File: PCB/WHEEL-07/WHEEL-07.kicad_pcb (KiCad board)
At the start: 2 copper layers, 11 parts, among them U1 STM32F405RGTx, Y1 16Mhz, Y2 32KHz

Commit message: Finished schematics
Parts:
- added C12: 0,1mF, Capacitor_SMD:C_0805_2012Metric, F.Cu at (103.8, 115.5)
- added C13: 1uF, Capacitor_SMD:C_0805_2012Metric, F.Cu at (127.5, 92.5)
- added C14: 4.7uF, Capacitor_SMD:C_0805_2012Metric, F.Cu at (127.5, 95.5)
- added IC1: TS5A21366DCUR, PDM_Additional:SOP50P310X90-8N, F.Cu at (104.4, 112.2)
- added R2: 2k2, Resistor_SMD:R_0402_1005Metric_Pad0.72x0.64mm_HandSolder, F.Cu at (109.2, 100.2)
- added R3: 2k2, Resistor_SMD:R_0402_1005Metric_Pad0.72x0.64mm_HandSolder, F.Cu at (116.5, 92.0)
- added R4: 120, Resistor_SMD:R_0402_1005Metric, F.Cu at (107.5, 115.0)
- added R5: 1k5, Resistor_SMD:R_0402_1005Metric_Pad0.72x0.64mm_HandSolder, F.Cu at (114.3, 96.8)
- added R6: 120, Resistor_SMD:R_0402_1005Metric, F.Cu at (103.1, 118.0)
- added U2: MCP2561-E-SN, Package_SO:SOIC-8_3.9x4.9mm_P1.27mm, F.Cu at (97.4, 113.6)
- added U3: MCP2561-E-SN, Package_SO:SOIC-8_3.9x4.9mm_P1.27mm, F.Cu at (97.4, 120.0)
- moved C8 54.5 mm to (119.7, 92.0)
- moved C4 51.2 mm to (119.7, 94.0)
- moved C3 44.7 mm to (109.2, 104.1)
- moved R1 44.7 mm to (116.5, 94.0)
- moved Y2 44.4 mm to (110.1, 97.5)
- moved U1 44.4 mm to (100.4, 98.2)
- moved Y1 44.4 mm to (111.2, 93.4)
- moved C9 43.0 mm to (117.5, 96.0)
- moved C7 41.8 mm to (112.5, 100.2)
- moved C5 40.8 mm to (112.5, 102.2)
- moved C6 40.6 mm to (109.2, 102.2)
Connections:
- U1 pad 10: unconnected-(U1-Pad10) -> ADC_A3
- U1 pad 11: unconnected-(U1-Pad11) -> ADC_A4
- U1 pad 14: unconnected-(U1-Pad14) -> ADC_B1
- U1 pad 15: unconnected-(U1-Pad15) -> ADC_B2
- U1 pad 16: unconnected-(U1-Pad16) -> ADC_B3
- U1 pad 17: unconnected-(U1-Pad17) -> ADC_B4
- U1 pad 2: unconnected-(U1-Pad2) -> LED_STATUS
- U1 pad 20: unconnected-(U1-Pad20) -> GPIO_1
- U1 pad 21: unconnected-(U1-Pad21) -> GPIO_2
- U1 pad 22: unconnected-(U1-Pad22) -> GPIO_3
- U1 pad 23: unconnected-(U1-Pad23) -> GPIO_4
- U1 pad 24: unconnected-(U1-Pad24) -> GPIO_5
- U1 pad 25: unconnected-(U1-Pad25) -> GPIO_6
- U1 pad 26: unconnected-(U1-Pad26) -> GPIO_7
- U1 pad 27: unconnected-(U1-Pad27) -> GPIO_8
- U1 pad 29: unconnected-(U1-Pad29) -> I2C2_SCL
- U1 pad 3: unconnected-(U1-Pad3) -> OSC32_IN
- U1 pad 30: unconnected-(U1-Pad30) -> I2C2_SDA
- U1 pad 34: unconnected-(U1-Pad34) -> SPI2_SCK
- U1 pad 35: unconnected-(U1-Pad35) -> SPI2_MISO
- U1 pad 36: unconnected-(U1-Pad36) -> SPI2_MOSI
- U1 pad 4: unconnected-(U1-Pad4) -> OSC32_OUT
- U1 pad 41: unconnected-(U1-Pad41) -> TIM1_CH1
- U1 pad 42: unconnected-(U1-Pad42) -> TIM1_CH2
- U1 pad 43: unconnected-(U1-Pad43) -> TIM1_CH3
- U1 pad 51: unconnected-(U1-Pad51) -> USART_TX
- U1 pad 52: unconnected-(U1-Pad52) -> USART_RX
- U1 pad 53: unconnected-(U1-Pad53) -> USART_CK
- U1 pad 57: unconnected-(U1-Pad57) -> CAN2_RX
- U1 pad 58: unconnected-(U1-Pad58) -> CAN2_TX
- U1 pad 61: unconnected-(U1-Pad61) -> CAN1_RX
- U1 pad 62: unconnected-(U1-Pad62) -> CAN1_TX
- U1 pad 8: unconnected-(U1-Pad8) -> ADC_A1
- U1 pad 9: unconnected-(U1-Pad9) -> ADC_A2

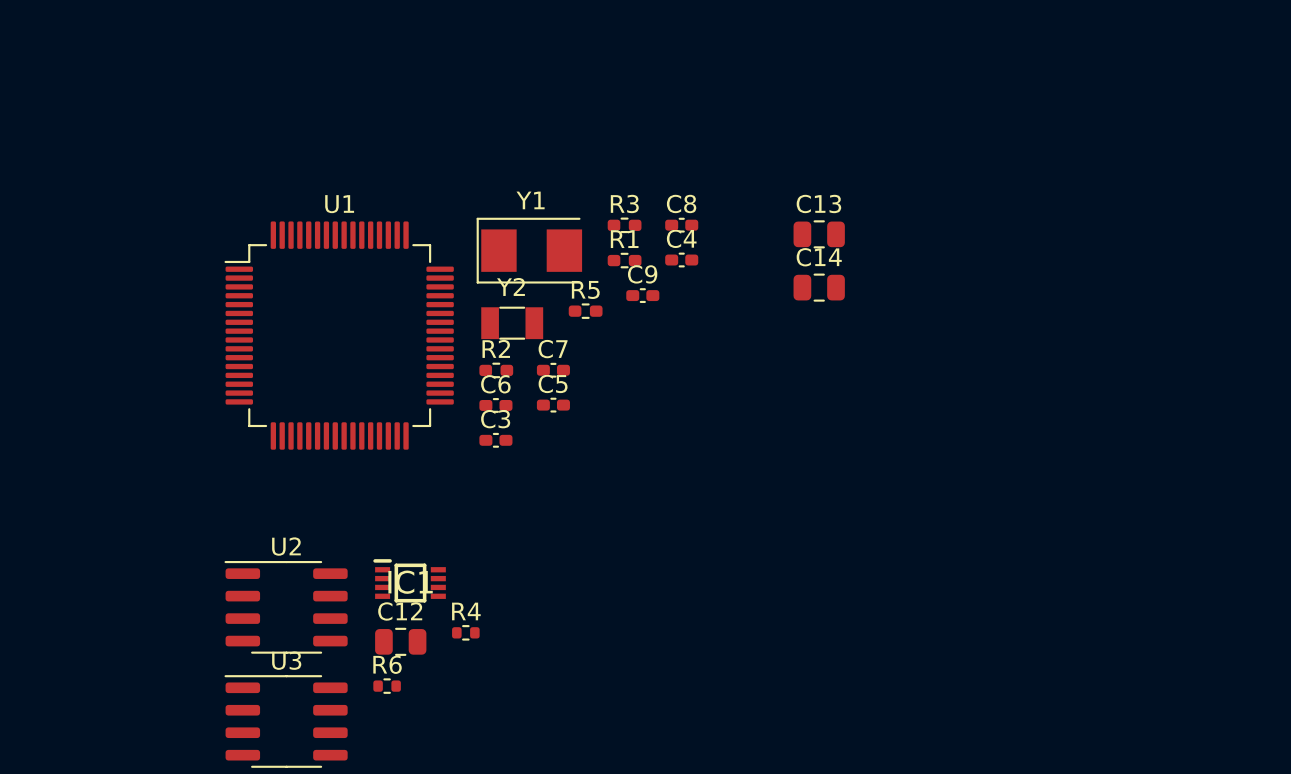
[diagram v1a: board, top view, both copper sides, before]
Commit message: Modified layout
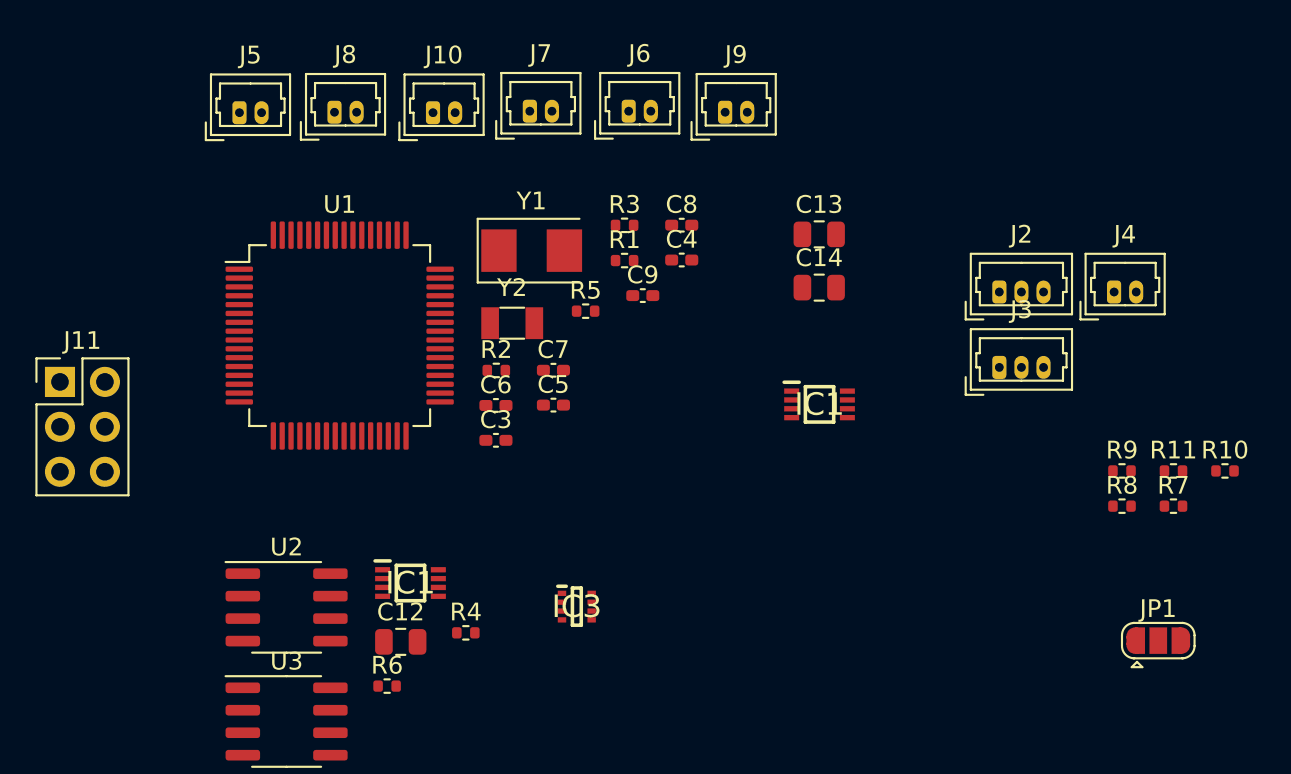
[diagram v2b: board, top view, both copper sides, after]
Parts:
- added IC1: TS5A21366DCUR, PDM_Additional:SOP50P310X90-8N, F.Cu at (127.5, 102.1)
- added IC3: MP2332HGTL-P, WHEEL_07_LIBRARY_LOADER:SOTFL50P160X60-8N, F.Cu at (113.8, 113.5)
- added J10: BUTTON, Connector_Molex:Molex_PicoBlade_53047-0210_1x02_P1.25mm_Vertical, F.Cu at (105.7, 85.6)
- added J11: Conn_02x03_Counter_Clockwise, Connector_PinHeader_2.54mm:PinHeader_2x03_P2.54mm_Vertical, F.Cu at (84.6, 100.8)
- added J2: SPI, Connector_Molex:Molex_PicoBlade_53047-0310_1x03_P1.25mm_Vertical, F.Cu at (137.7, 95.8)
- added J3: USART, Connector_Molex:Molex_PicoBlade_53047-0310_1x03_P1.25mm_Vertical, F.Cu at (137.7, 100.0)
- added J4: I2C, Connector_Molex:Molex_PicoBlade_53047-0210_1x02_P1.25mm_Vertical, F.Cu at (144.2, 95.8)
- added J5: BUTTON, Connector_Molex:Molex_PicoBlade_53047-0210_1x02_P1.25mm_Vertical, F.Cu at (94.7, 85.6)
- added J6: BUTTON, Connector_Molex:Molex_PicoBlade_53047-0210_1x02_P1.25mm_Vertical, F.Cu at (116.7, 85.5)
- added J7: BUTTON, Connector_Molex:Molex_PicoBlade_53047-0210_1x02_P1.25mm_Vertical, F.Cu at (111.1, 85.5)
- added J8: BUTTON, Connector_Molex:Molex_PicoBlade_53047-0210_1x02_P1.25mm_Vertical, F.Cu at (100.1, 85.6)
- added J9: BUTTON, Connector_Molex:Molex_PicoBlade_53047-0210_1x02_P1.25mm_Vertical, F.Cu at (122.2, 85.6)
- added JP1: SolderJumper_3_Open, Jumper:SolderJumper-3_P1.3mm_Open_RoundedPad1.0x1.5mm, F.Cu at (146.7, 115.5)
- added R10: 13k, Resistor_SMD:R_0402_1005Metric, F.Cu at (150.4, 105.9)
- added R11: 40.2k, Resistor_SMD:R_0402_1005Metric, F.Cu at (147.5, 105.9)
- added R7: 200k, Resistor_SMD:R_0402_1005Metric, F.Cu at (147.5, 107.9)
- added R8: 20, Resistor_SMD:R_0402_1005Metric, F.Cu at (144.6, 107.9)
- added R9: 20k, Resistor_SMD:R_0402_1005Metric, F.Cu at (144.6, 105.9)
- R1, R2, R3, R5: footprint Resistor_SMD:R_0402_1005Metric_Pad0.72x0.64mm_HandSolder -> Resistor_SMD:R_0402_1005Metric
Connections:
- C8 pad 1: VDDA -> +3.3VA
- C9 pad 1: VDDA -> +3.3VA
- IC1 pad 3: /CAN_BUS/CAN_TERMINATOR_2 -> CAN2_TERMINATOR_SW
- IC1 pad 7: /CAN_BUS/CAN_TERMINATOR_1 -> CAN1_TERMINATOR_SW
- R4 pad 2: Net-(IC1-Pad1) -> Net-(R4-Pad2)
- R6 pad 2: Net-(IC1-Pad5) -> Net-(R6-Pad2)
- U1 pad 33: unconnected-(U1-Pad33) -> SPI_CS
- U1 pad 37: unconnected-(U1-Pad37) -> TIM1_CH1
- U1 pad 38: unconnected-(U1-Pad38) -> TIM1_CH2
- U1 pad 39: unconnected-(U1-Pad39) -> TIM1_CH3
- U1 pad 56: unconnected-(U1-Pad56) -> CAN2_TERMINATOR_SW
- U1 pad 59: unconnected-(U1-Pad59) -> CAN1_TERMINATOR_SW
- U1 pad 63: unconnected-(U1-Pad63) -> GND

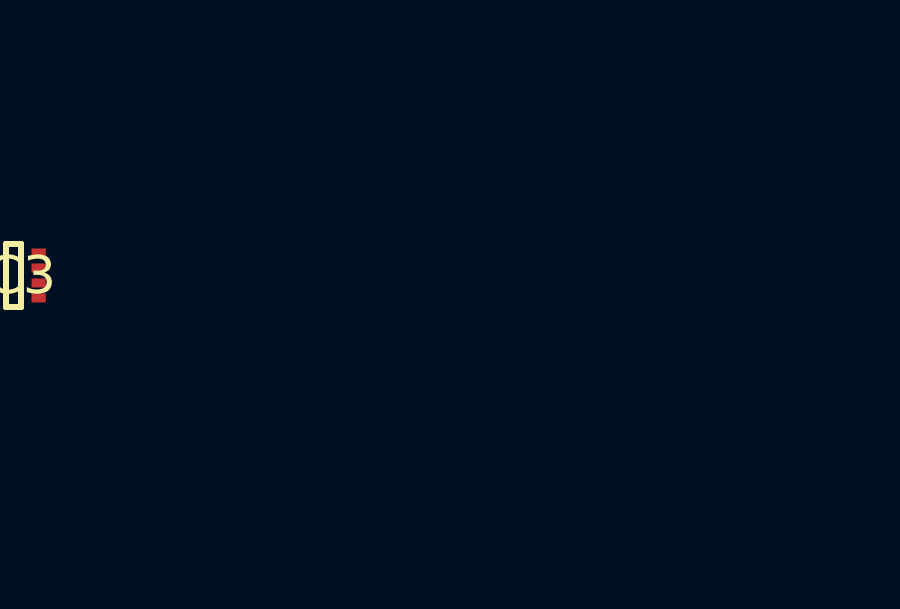
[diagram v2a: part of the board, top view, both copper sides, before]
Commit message: Added paddles hardware debouncing to PCB
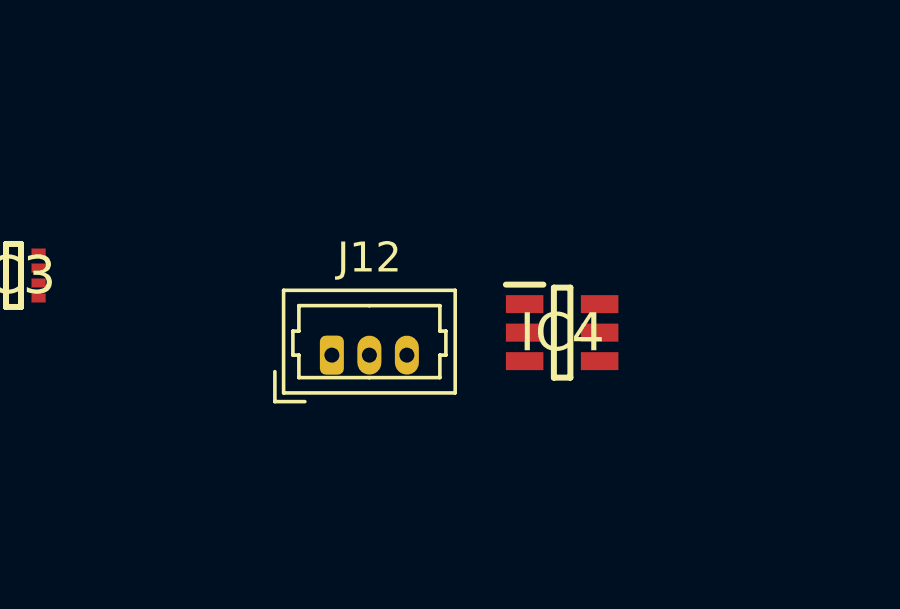
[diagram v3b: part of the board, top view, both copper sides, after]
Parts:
- added IC4: NL27WZ14DTT1G, WHEEL_07_LIBRARY_LOADER:SOT95P275X110-6N, F.Cu at (132.1, 115.4)
- added J12: USART, Connector_Molex:Molex_PicoBlade_53047-0310_1x03_P1.25mm_Vertical, F.Cu at (124.4, 116.2)
- J5: value BUTTON -> PADDLE1
- J6: value BUTTON -> PADDLE2
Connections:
- IC1 pad 1: Net-(R4-Pad2) -> Net-(IC1-Pad1)
- IC1 pad 5: Net-(R6-Pad2) -> Net-(IC1-Pad5)
- J5 pad 2: GPIO_1 -> PADDLE1_IN
- J6 pad 2: GPIO_2 -> PADDLE2_IN
- R4 pad 2: Net-(R4-Pad2) -> Net-(IC1-Pad1)
- R6 pad 2: Net-(R6-Pad2) -> Net-(IC1-Pad5)

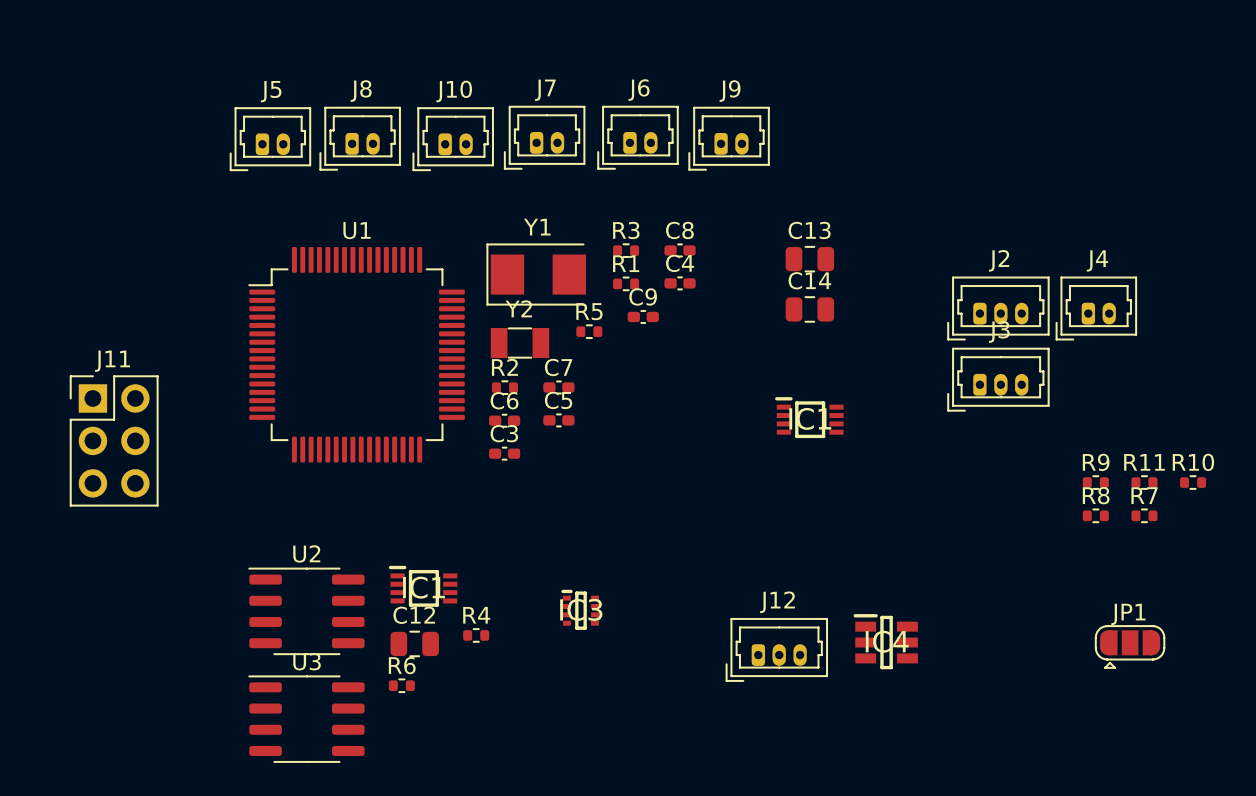
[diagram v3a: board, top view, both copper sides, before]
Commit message: Added rotaries
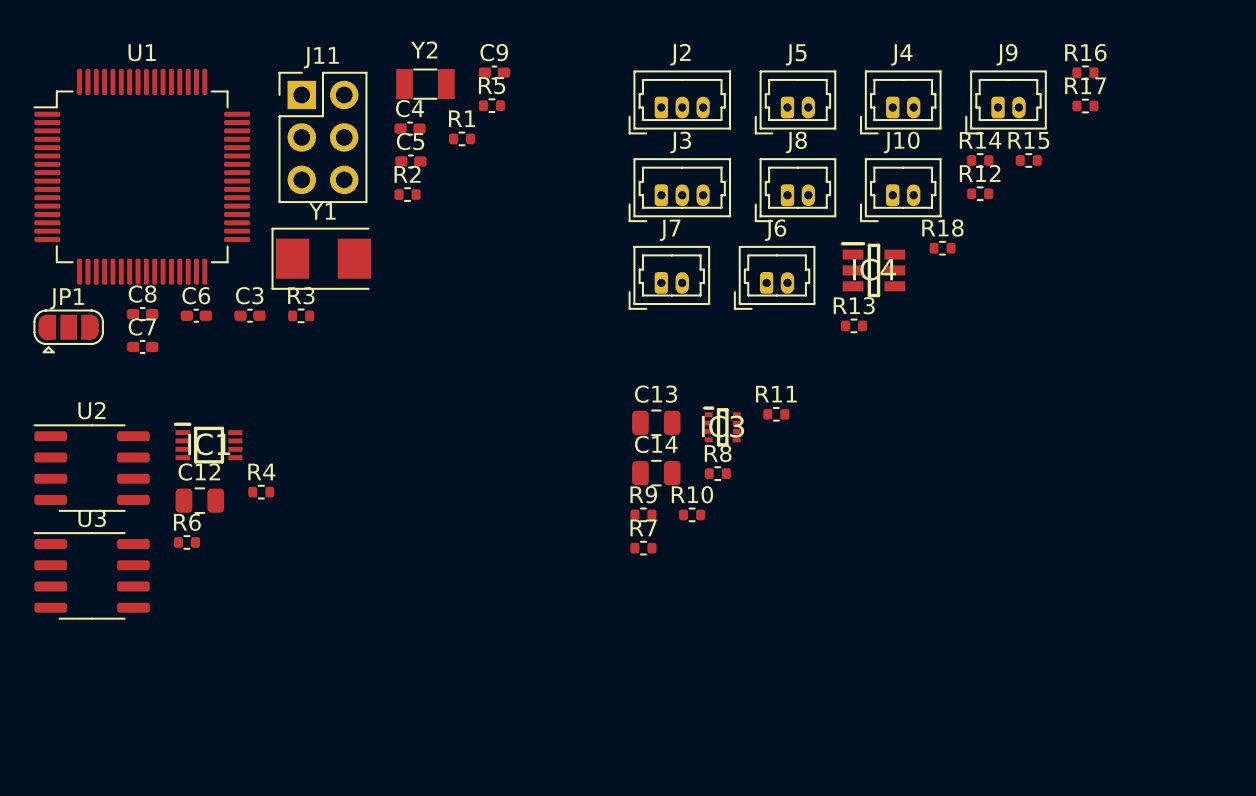
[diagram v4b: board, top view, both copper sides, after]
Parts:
- removed the IC1 at (104.4, 112.2)
- removed the IC1 at (127.5, 102.1)
- removed J12: USART, Connector_Molex:Molex_PicoBlade_53047-0310_1x03_P1.25mm_Vertical
- added IC1: TS5A21366DCUR, PDM_Additional:SOP50P310X90-8N, F.Cu at (91.5, 103.6)
- added R12: 1k, Resistor_SMD:R_0402_1005Metric, F.Cu at (137.7, 88.6)
- added R13: 1k, Resistor_SMD:R_0402_1005Metric, F.Cu at (130.1, 96.5)
- added R14: 10k, Resistor_SMD:R_0402_1005Metric, F.Cu at (137.7, 86.6)
- added R15: 10k, Resistor_SMD:R_0402_1005Metric, F.Cu at (140.6, 86.6)
- added R16: 1k, Resistor_SMD:R_0402_1005Metric, F.Cu at (144.0, 81.3)
- added R17: 1k, Resistor_SMD:R_0402_1005Metric, F.Cu at (144.0, 83.3)
- added R18: 1k, Resistor_SMD:R_0402_1005Metric, F.Cu at (135.4, 91.8)
- moved JP1 66.3 mm to (83.1, 96.6)
- moved C8 32.4 mm to (87.6, 95.8)
- moved J5 31.5 mm to (126.2, 83.4)
- moved R10 30.0 mm to (120.4, 107.8)
- moved R7 30.0 mm to (117.5, 109.8)
- moved R9 27.1 mm to (117.5, 107.8)
- moved J10 27.0 mm to (132.4, 88.7)
- moved J8 26.2 mm to (126.2, 88.7)
- moved C7 25.0 mm to (87.6, 97.8)
- moved R8 22.8 mm to (122.0, 105.3)
- moved J2 22.7 mm to (118.6, 83.4)
- moved R11 22.4 mm to (125.5, 101.8)
- moved IC4 22.3 mm to (131.3, 93.2)
- moved J3 22.2 mm to (118.6, 88.7)
- moved J11 22.0 mm to (97.1, 82.7)
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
